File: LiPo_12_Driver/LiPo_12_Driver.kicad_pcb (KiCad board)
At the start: 2 copper layers, 58 parts, among them Q1 NMOS, Q2 NMOS, Q3 NMOS, Q4 NMOS, Q5 NMOS, Q6 NMOS, Q7 NMOS, U1 TI_LM5175

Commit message: more lipo pcb dev
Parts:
- Q1, Q2, Q3, Q4, Q5, Q6, Q7: value NMOS -> Q_NMOS
- moved C23 142.1 mm to (168.7, 79.0), turned to 270 degrees
- moved C26 121.6 mm to (158.5, 70.4), turned to 90 degrees
- moved C20 112.9 mm to (155.2, 75.4), turned to 270 degrees
- moved C24 109.6 mm to (158.5, 75.4), turned to 270 degrees
- moved C27 109.6 mm to (161.8, 70.4), turned to 90 degrees
- moved C16 109.3 mm to (142.5, 74.2), turned to 270 degrees
- moved C18 108.9 mm to (149.6, 68.1), turned to 90 degrees
- moved C17 108.8 mm to (142.5, 64.5), turned to 90 degrees
- moved C25 107.4 mm to (161.8, 75.4), turned to 270 degrees
- moved C22 105.6 mm to (167.1, 79.0), turned to 270 degrees
- moved J4 101.6 mm to (173.0, 95.0)
- moved C19 97.8 mm to (151.9, 75.4), turned to 270 degrees
- moved C21 93.1 mm to (155.2, 70.4), turned to 90 degrees
- moved J1 88.0 mm to (172.7, 78.2)
- moved Q5 78.7 mm to (128.6, 63.1)
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- renumbered OUT+ to J1, GND to J2, VIN+ to J3, GND to J4
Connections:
- Q1 pad 1: Net-(Q1-Pad1) -> Net-(C13-Pad1)
- Q1 pad 2: +VDC -> Net-(Q1-Pad2)
- Q1 pad 3: Net-(C13-Pad1) -> +VDC
- Q2 pad 1: Net-(Q1-Pad1) -> Net-(C13-Pad1)
- Q2 pad 2: +VDC -> Net-(Q1-Pad2)
- Q2 pad 3: Net-(C13-Pad1) -> +VDC
- Q3 pad 1: Net-(Q3-Pad1) -> Net-(D3-Pad2)
- Q3 pad 2: Net-(C13-Pad1) -> Net-(Q3-Pad2)
- Q3 pad 3: Net-(D3-Pad2) -> Net-(C13-Pad1)
- Q4 pad 1: HDRV2 -> SW2
- Q4 pad 2: VOSNS -> HDRV2
- Q4 pad 3: SW2 -> VOSNS
- Q5 pad 1: HDRV2 -> SW2
- Q5 pad 2: VOSNS -> HDRV2
- Q5 pad 3: SW2 -> VOSNS
- Q6 pad 1: LDRV2 -> Net-(D3-Pad2)
- Q6 pad 2: SW2 -> LDRV2
- Q6 pad 3: Net-(D3-Pad2) -> SW2
- Q7 pad 1: LDRV2 -> Net-(D3-Pad2)
- Q7 pad 2: SW2 -> LDRV2
- Q7 pad 3: Net-(D3-Pad2) -> SW2
- U1 pad 1: Net-(R2-Pad2) -> Net-(R12-Pad2)
- U1 pad 11: Net-(R7-Pad1) -> GND
- U1 pad 12: VOSNS -> Net-(C14-Pad1)
- U1 pad 13: GND -> Net-(C14-Pad2)
- U1 pad 14: GND -> Net-(R4-Pad1)
- U1 pad 15: Net-(C14-Pad1) -> SW2
- U1 pad 16: Net-(C14-Pad2) -> HDRV2
- U1 pad 17: Net-(R4-Pad1) -> BOOT2
- U1 pad 18: SW2 -> LDRV2
- U1 pad 19: HDRV2 -> GND
- U1 pad 2: Net-(C12-Pad2) -> GND
- U1 pad 20: BOOT2 -> Net-(C8-Pad2)
- U1 pad 21: LDRV2 -> Net-(C7-Pad2)
- U1 pad 22: GND -> Net-(Q3-Pad2)
- U1 pad 23: Net-(C8-Pad2) -> Net-(C13-Pad2)
- U1 pad 24: Net-(C7-Pad2) -> Net-(Q1-Pad2)
- U1 pad 25: Net-(Q3-Pad1) -> Net-(C13-Pad1)
- U1 pad 26: Net-(C13-Pad2) -> Net-(R2-Pad2)
- U1 pad 27: Net-(Q1-Pad1) -> Net-(C12-Pad2)
- U1 pad 28: Net-(C13-Pad1) -> +VDC
- U1 pad 3: +VDC -> Net-(R1-Pad1)
- U1 pad 4: Net-(R12-Pad2) -> Net-(C10-Pad2)
- U1 pad 5: GND -> Net-(C6-Pad2)
- U1 pad 6: Net-(R1-Pad1) -> Net-(C11-Pad2)
- U1 pad 7: Net-(C10-Pad2) -> GND
- U1 pad 8: Net-(C6-Pad2) -> Net-(R7-Pad1)
- U1 pad 9: Net-(C11-Pad2) -> VOSNS
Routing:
- net Net-(C12-Pad2): track 0.00 -> 6.93 mm
- net Net-(D1-Pad1): track 0.00 -> 1.79 mm

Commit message: More LIPO PCB development
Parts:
- moved R9 77.3 mm to (84.8, 101.1), turned to 180 degrees
- moved R11 75.2 mm to (90.9, 97.0), turned to 90 degrees
- moved R10 68.0 mm to (84.8, 93.7), turned to 180 degrees
- moved R7 57.2 mm to (103.4, 88.1)
- moved R8 56.6 mm to (99.8, 88.1)
- moved D4 54.8 mm to (132.3, 81.0), turned to 270 degrees
- moved Q3 50.0 mm to (103.9, 98.0), turned to 90 degrees
- moved Q6 45.3 mm to (130.0, 87.9)
- moved Q7 45.3 mm to (134.1, 87.9)
- moved R5 42.1 mm to (103.9, 73.4)
- moved U1 41.8 mm to (104.6, 80.8)
- moved D3 41.3 mm to (97.3, 96.0), turned to 90 degrees
- moved C1 35.1 mm to (72.6, 64.5)
- moved J2 35.1 mm to (64.5, 73.7)
- moved J3 35.1 mm to (64.5, 65.8)
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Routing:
- net VOSNS: track 0.00 -> 135.3 mm, vias 0 -> 2
- net SW2: track 0.00 -> 79.1 mm
- net +VDC: track 0.00 -> 24.7 mm
- net Net-(D1-Pad1): track 1.79 -> 16.7 mm
- net Net-(C12-Pad2): track 6.93 -> 4.05 mm

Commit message: Almost finished LIPO PCB
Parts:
- moved R12 93.3 mm to (108.2, 66.6), turned to 90 degrees
- moved C6 93.0 mm to (112.3, 66.6), turned to 90 degrees
- moved R6 86.9 mm to (118.2, 67.4), turned to 270 degrees
- moved R1 67.9 mm to (109.5, 65.9), turned to 270 degrees
- moved C11 55.1 mm to (115.3, 66.6), turned to 90 degrees
- moved R9 54.5 mm to (126.2, 65.6), turned to 270 degrees
- moved D5 54.3 mm to (112.7, 53.3), turned to 90 degrees
- moved R2 51.8 mm to (106.9, 62.3)
- moved R10 51.3 mm to (127.7, 65.6), turned to 270 degrees
- moved C9 49.6 mm to (113.8, 66.6), turned to 90 degrees
- moved C10 48.8 mm to (110.7, 66.7), turned to 90 degrees
- moved C15 47.6 mm to (114.9, 53.8), turned to 270 degrees
- moved D2 45.5 mm to (110.3, 53.3), turned to 90 degrees
- moved R3 45.5 mm to (106.9, 63.3), turned to 180 degrees
- moved C8 45.1 mm to (103.3, 60.2), turned to 90 degrees
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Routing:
- net VOSNS: track 135.3 -> 23.4 mm, vias 2 -> 4
- net SW2: track 79.1 -> 5.54 mm, vias 0 -> 26
- net Net-(D3-Pad2): track 0.00 -> 67.9 mm, vias 0 -> 20
- net LDRV2: track 0.00 -> 19.0 mm, vias 0 -> 4
- net Net-(Q1-Pad2): track 0.00 -> 18.3 mm, vias 0 -> 3
- net Net-(Q3-Pad2): track 0.00 -> 18.0 mm, vias 0 -> 2
- net Net-(C12-Pad2): track 4.05 -> 20.6 mm, vias 0 -> 2
- net Net-(C14-Pad2): track 0.00 -> 16.4 mm, vias 0 -> 2
- net Net-(C14-Pad1): track 0.00 -> 15.7 mm, vias 0 -> 2
- net HDRV2: track 0.00 -> 15.4 mm, vias 0 -> 3
- net Net-(D1-Pad1): track 16.7 -> 1.67 mm
- net Net-(C13-Pad1): track 0.00 -> 11.1 mm
- net Net-(C13-Pad2): track 0.00 -> 11.0 mm, vias 0 -> 2
- net Net-(C8-Pad2): track 0.00 -> 9.88 mm, vias 0 -> 2
- net BOOT2: track 0.00 -> 8.42 mm
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- added copper zone on F.Cu, net +VDC
- added copper zone on B.Cu, net GND
- added copper zone on F.Cu, net GND
- added copper zone on F.Cu, net Net-(C13-Pad1)
- added copper zone on B.Cu, net SW2
- added copper zone on F.Cu, net SW2
- added copper zone on F.Cu, net VOSNS
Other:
- board outline added: 90.4 x 56.4 mm
- net class Default: trace_width 0.25 -> 0.2
- rule trace_min: 0.2 -> 0.127
- rule via_min_drill: 0.3 -> 0.2

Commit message: Finished LIPO Driver PCB
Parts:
- J1: value M+ -> VOUT
- J3: value VIN+ -> VIN
- moved C17 9.82 mm to (138.4, 72.4)
- moved C16 7.62 mm to (134.8, 44.4)
- moved C18 7.62 mm to (142.0, 44.4)
- moved C22 7.62 mm to (156.1, 47.5)
- moved C24 7.62 mm to (147.2, 46.7)
- moved C25 7.62 mm to (150.4, 46.7)
- moved C27 7.62 mm to (153.7, 46.7)
- moved C19 7.62 mm to (143.9, 73.3)
- moved C20 7.62 mm to (147.2, 73.3)
- moved C21 7.62 mm to (150.5, 73.3)
- moved C23 7.62 mm to (156.1, 72.5)
- moved C26 7.62 mm to (153.7, 73.3)
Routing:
- net GND: track 3.99 -> 18.1 mm, vias 77 -> 120
- net Net-(D3-Pad2): track 67.9 -> 72.8 mm, vias 20 -> 22
- net LDRV2: track 19.0 -> 18.2 mm, vias 4 -> 5
- net SW2: vias 26 -> 18

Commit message: Small updates, Ready for order
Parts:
- moved C16 50.1 mm to (160.2, 87.6)
- moved C18 50.1 mm to (167.4, 87.6)
- moved C22 50.1 mm to (181.5, 90.7)
- moved C25 50.1 mm to (175.8, 89.9)
- moved C27 50.1 mm to (179.1, 89.9)
- moved C24 50.1 mm to (172.6, 89.9)
- moved Q4 48.1 mm to (148.7, 90.6)
- moved Q7 48.1 mm to (148.7, 98.7)
- moved Q5 48.1 mm to (148.7, 94.7)
- moved Q6 48.1 mm to (148.7, 102.8)
- moved C10 48.1 mm to (136.1, 107.6)
- moved C7 48.1 mm to (130.7, 97.3)
- moved D4 48.1 mm to (154.6, 100.2)
- moved J3 48.1 mm to (101.5, 95.5)
- moved Q3 48.1 mm to (122.3, 102.5)
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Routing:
- net GND: vias 120 -> 131

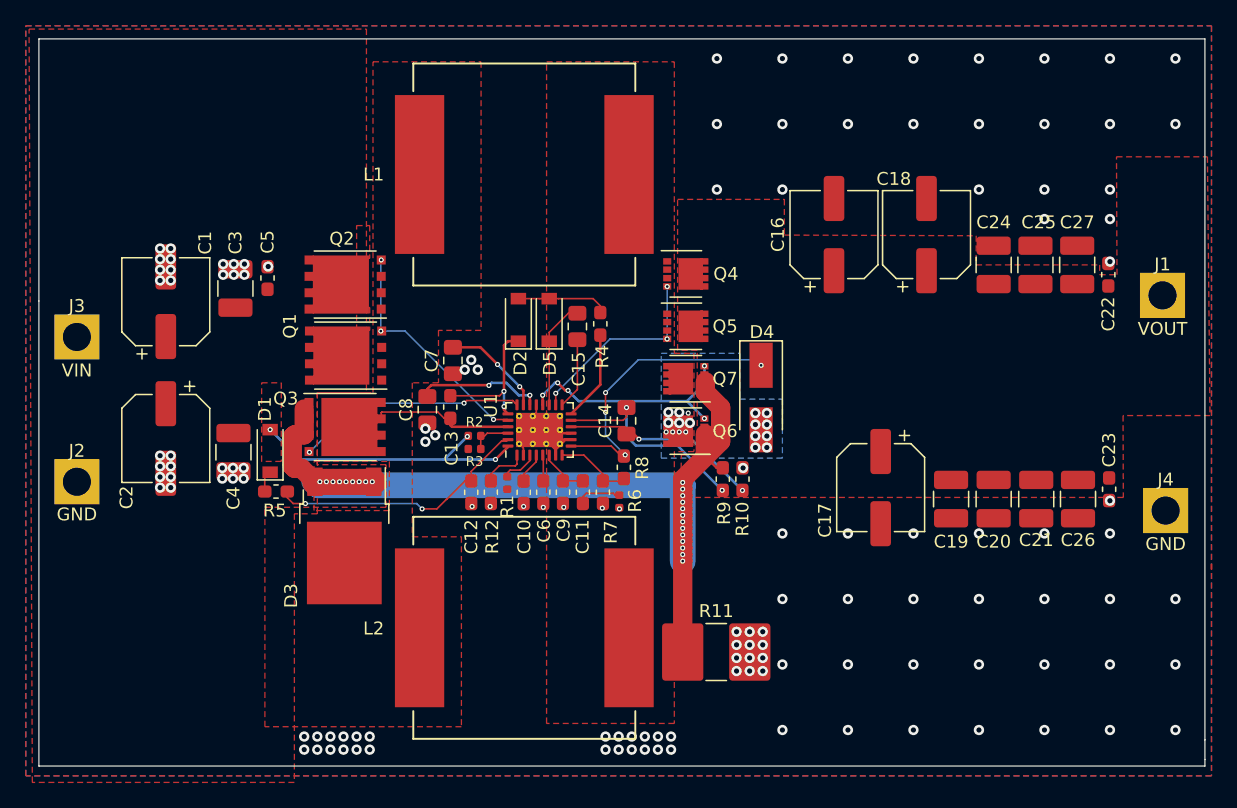
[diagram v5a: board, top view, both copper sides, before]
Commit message: Updated PCB because QFN package is out of stockaslhdflsakghlksa
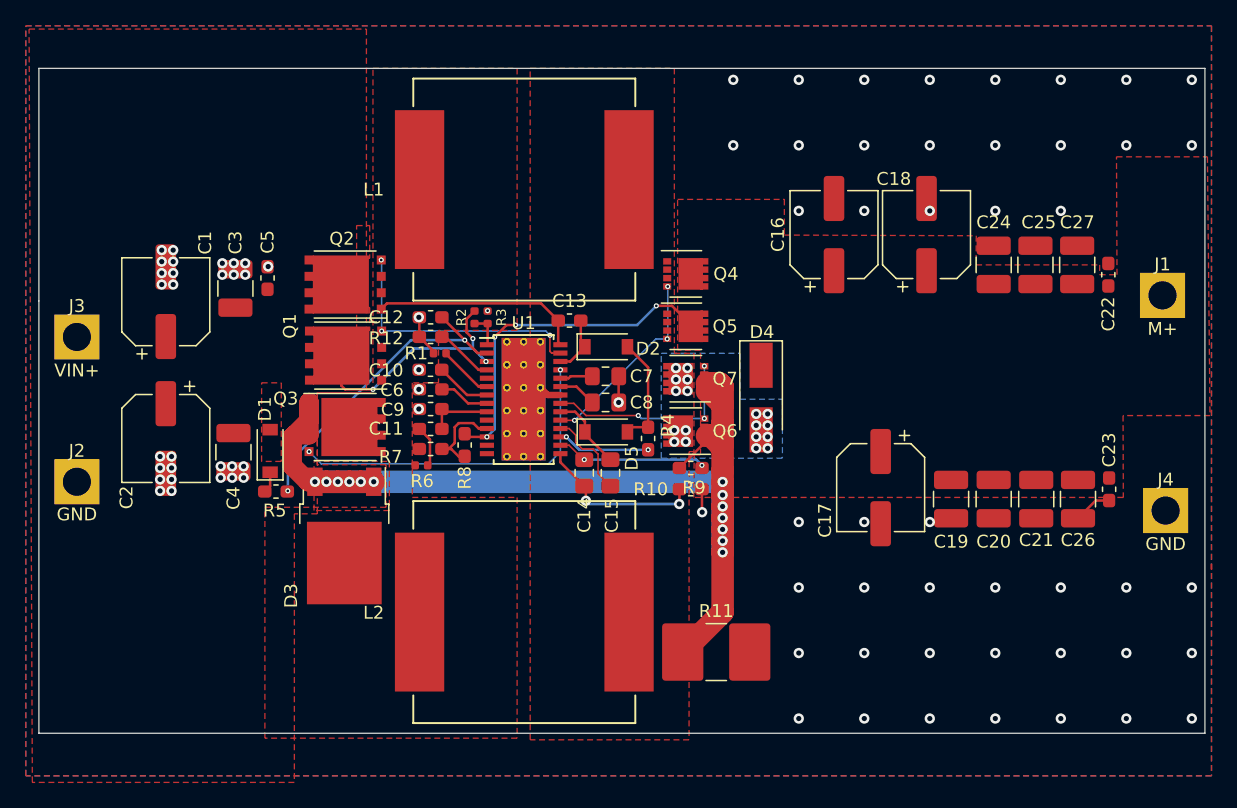
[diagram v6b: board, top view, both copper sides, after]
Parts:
- J1: value VOUT -> M+
- J3: value VIN -> VIN+
- U1: value TI_LM5175 -> TI_LM5175_HSSOP; footprint Package_DFN_QFN:QFN-28-1EP_4x5mm_P0.5mm_EP2.65x3.65mm_ThermalVias -> Package_SO:HTSSOP-28-1EP_4.4x9.7mm_P0.65mm_EP3.4x9.5mm_ThermalVias
- moved R6 15.6 mm to (128.2, 105.5), turned to 180 degrees
- moved C12 13.9 mm to (128.9, 94.0), turned to 0 degrees
- moved C8 13.8 mm to (142.5, 100.6), turned to 180 degrees
- moved R7 13.8 mm to (128.9, 104.2), turned to 180 degrees
- moved R12 12.9 mm to (128.9, 95.5), turned to 0 degrees
- moved C11 12.8 mm to (128.9, 102.6), turned to 0 degrees
- moved R8 12.5 mm to (131.6, 103.9)
- moved C9 12.1 mm to (128.9, 101.1), turned to 0 degrees
- moved C10 11.9 mm to (128.9, 98.0), turned to 0 degrees
- moved C7 11.9 mm to (142.5, 98.6), turned to 180 degrees
- moved C6 11.8 mm to (128.9, 99.6), turned to 0 degrees
- moved C15 11.6 mm to (142.9, 106.0)
- moved C13 11.4 mm to (139.7, 94.2), turned to 0 degrees
- moved R1 11.3 mm to (129.6, 96.8), turned to 180 degrees
- moved R3 10.3 mm to (133.3, 94.0), turned to 90 degrees
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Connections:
- U1 pad 1: Net-(R12-Pad2) -> Net-(R2-Pad2)
- U1 pad 11: GND -> Net-(R7-Pad1)
- U1 pad 12: Net-(C14-Pad1) -> VOSNS
- U1 pad 13: Net-(C14-Pad2) -> GND
- U1 pad 14: Net-(R4-Pad1) -> GND
- U1 pad 15: SW2 -> Net-(C14-Pad1)
- U1 pad 16: HDRV2 -> Net-(C14-Pad2)
- U1 pad 17: BOOT2 -> Net-(R4-Pad1)
- U1 pad 18: LDRV2 -> SW2
- U1 pad 19: GND -> HDRV2
- U1 pad 2: GND -> Net-(C12-Pad2)
- U1 pad 20: Net-(C8-Pad2) -> BOOT2
- U1 pad 21: Net-(C7-Pad2) -> LDRV2
- U1 pad 22: Net-(Q3-Pad2) -> GND
- U1 pad 23: Net-(C13-Pad2) -> Net-(C8-Pad2)
- U1 pad 24: Net-(Q1-Pad2) -> Net-(C7-Pad2)
- U1 pad 25: Net-(C13-Pad1) -> Net-(Q3-Pad2)
- U1 pad 26: Net-(R2-Pad2) -> Net-(C13-Pad2)
- U1 pad 27: Net-(C12-Pad2) -> Net-(Q1-Pad2)
- U1 pad 28: +VDC -> Net-(C13-Pad1)
- U1 pad 3: Net-(R1-Pad1) -> +VDC
- U1 pad 4: Net-(C10-Pad2) -> Net-(R12-Pad2)
- U1 pad 5: Net-(C6-Pad2) -> GND
- U1 pad 6: Net-(C11-Pad2) -> Net-(R1-Pad1)
- U1 pad 7: GND -> Net-(C10-Pad2)
- U1 pad 8: Net-(R7-Pad1) -> Net-(C6-Pad2)
- U1 pad 9: VOSNS -> Net-(C11-Pad2)
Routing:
- net Net-(D3-Pad2): track 72.8 -> 83.9 mm, vias 22 -> 13
- net Net-(Q3-Pad2): track 18.0 -> 26.6 mm
- net Net-(C8-Pad2): track 9.88 -> 2.98 mm, vias 2 -> 0
- net Net-(C13-Pad2): track 11.0 -> 4.54 mm, vias 2 -> 0
- net GND: track 18.1 -> 11.9 mm, vias 131 -> 81
- net Net-(C7-Pad2): track 7.97 -> 2.54 mm, vias 2 -> 0
- net Net-(C13-Pad1): track 11.1 -> 16.4 mm
- net Net-(C14-Pad2): track 16.4 -> 11.6 mm
- net Net-(C12-Pad2): track 20.6 -> 24.5 mm
- net +VDC: track 22.6 -> 18.8 mm
- net Net-(C14-Pad1): track 15.7 -> 13.0 mm
- net VOSNS: track 23.4 -> 26.0 mm
- net Net-(Q1-Pad2): track 18.3 -> 20.8 mm
- net LDRV2: track 18.2 -> 15.7 mm, vias 5 -> 3
- net BOOT2: track 8.42 -> 5.99 mm
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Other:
- board size 90.4 x 56.4 mm -> 90.4 x 51.6 mm

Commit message: LIPO gerbers generated
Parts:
- moved J4 4.95 mm to (181.0, 109.0)
- moved J1 4.78 mm to (180.9, 92.3)
- moved C17 3.69 mm to (160.1, 107.1)
- moved C21 3.69 mm to (172.2, 108.0)
- moved C23 3.69 mm to (177.9, 107.2)
- moved C16 3.69 mm to (156.5, 87.4)
- moved C18 3.69 mm to (163.7, 87.4)
- moved C19 3.69 mm to (165.6, 108.0)
- moved C20 3.69 mm to (168.9, 108.0)
- moved C22 3.69 mm to (177.8, 90.6)
- moved C24 3.69 mm to (168.9, 89.8)
- moved C25 3.69 mm to (172.1, 89.8)
- moved C26 3.69 mm to (175.5, 108.0)
- moved C27 3.69 mm to (175.4, 89.8)
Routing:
- net GND: vias 81 -> 75
- net VOSNS: vias 4 -> 5
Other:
- board size 90.4 x 51.6 mm -> 84.6 x 51.6 mm
- board text added: "JLCJLCJLCJLC"
- board text added: "RoboBooster 12V - 240W Edition Designed by Yousif Alfraji"
